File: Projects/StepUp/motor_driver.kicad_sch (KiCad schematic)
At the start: 39 parts, among them J5 TBLH10-350-04BK, Q1 BSS84, Q2 2N7002, U4 TMC2300-LA

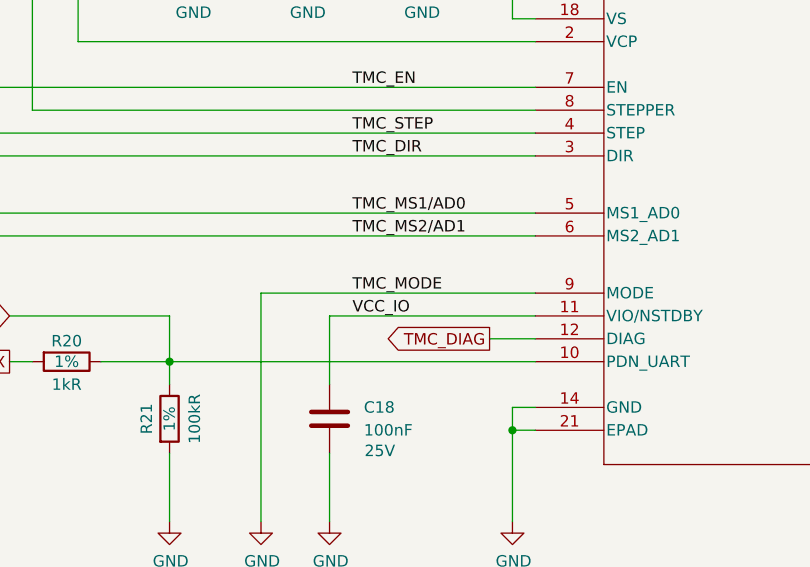
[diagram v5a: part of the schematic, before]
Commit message: chore(pins): MCU_BOOST_EN to MCU, fixed errors
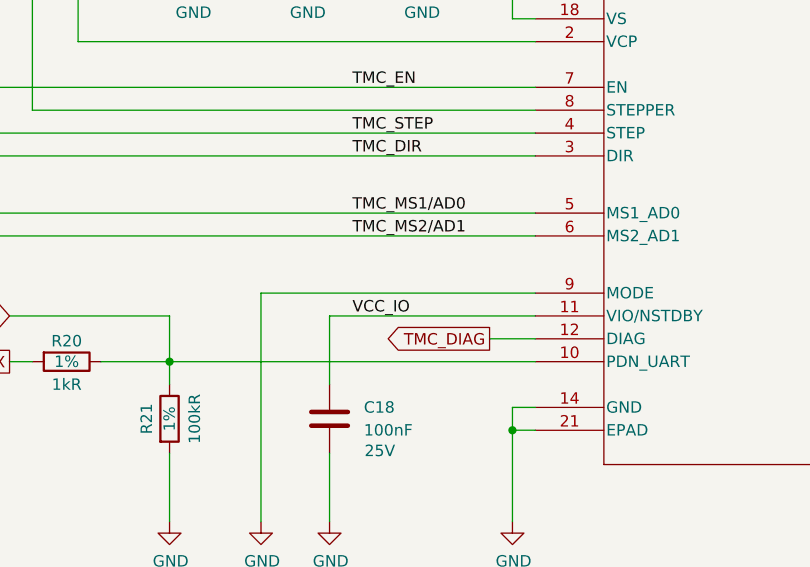
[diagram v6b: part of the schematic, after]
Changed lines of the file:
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@@
 		)
 	)
-	(label "TMC_MODE"
-		(at 124.46 177.8 0)
-		(fields_autoplaced yes)
-		(effects
-			(font
-				(size 1.27 1.27)
-			)
-			(justify left bottom)
-		)
-	)
 	(label "OB1_OUT"
 		(at 307.34 160.02 0)
@@
 			(font
 				(size 1.27 1.27)
+				(color 194 0 194 1)
 			)
 			(justify right)
@@
 			(font
 				(size 1.27 1.27)
+				(color 194 0 194 1)
 			)
 			(justify right)
@@
 			(font
 				(size 1.27 1.27)
+				(color 194 0 194 1)
 			)
 			(justify right)
@@
 			(font
 				(size 1.27 1.27)
+				(color 194 0 194 1)
 			)
 			(justify right)
@@
 			(font
 				(size 1.27 1.27)
+				(color 194 0 194 1)
 			)
 			(justify right)
@@
 			(font
 				(size 1.27 1.27)
+				(color 194 0 194 1)
 			)
 			(justify right)
@@
 			(font
 				(size 1.27 1.27)
+				(color 194 0 194 1)
 			)
 			(justify right)
@@
 			)
 		)
-		(property "Description" ""
+		(property "Description" "Power symbol creates a global label with name \"GND\" , ground"
 			(at 132.08 142.24 0)
 			(effects
@@
 			)
 		)
-		(property "Description" ""
+		(property "Description" "Power symbol creates a global label with name \"GND\" , ground"
 			(at 76.2 86.36 0)
 			(effects
@@
 			)
 		)
-		(property "Description" ""
+		(property "Description" "Power symbol creates a global label with name \"GND\" , ground"
 			(at 114.3 203.2 0)
 			(effects
@@
 			)
 		)
-		(property "Description" ""
+		(property "Description" "Power symbol creates a global label with name \"GND\" , ground"
 			(at 63.5 86.36 0)
 			(effects
@@
 			)
 		)
-		(property "Description" ""
+		(property "Description" "Power symbol creates a global label with name \"GND\" , ground"
 			(at 63.5 190.5 0)
 			(effects
@@
 			)
 		)
-		(property "Description" ""
+		(property "Description" "Power symbol creates a global label with name \"GND\" , ground"
 			(at 119.38 142.24 0)
 			(effects
@@
 			)
 		)
-		(property "Description" ""
+		(property "Description" "Power symbol creates a global label with name \"GND\" , ground"
 			(at 264.16 154.94 0)
 			(effects
@@
 			)
 		)
-		(property "Description" ""
+		(property "Description" "Power symbol creates a global label with name \"GND\" , ground"
 			(at 104.14 203.2 0)
 			(effects
@@
 			)
 		)
-		(property "Description" ""
+		(property "Description" "Power symbol creates a global label with name \"GND\" , ground"
 			(at 269.24 185.42 0)
 			(effects
@@
 			)
 		)
-		(property "Description" ""
+		(property "Description" "Power symbol creates a global label with name \"GND\" , ground"
 			(at 358.14 182.88 0)
 			(effects
@@
 			)
 		)
+		(property "Description" "MOSFET P-CH 50V 130MA SOT-23"
+			(at 35.56 40.64 0)
+			(effects
+				(font
+					(size 1.524 1.524)
+				)
+				(justify left)
+				(hide yes)
+			)
+		)
 		(pin "3"
 		)
@@
 			)
 		)
-		(property "Description" ""
+		(property "Description" "Power symbol creates a global label with name \"GND\" , ground"
 			(at 121.92 203.2 0)
 			(effects
@@
 			)
 		)
-		(property "Description" ""
+		(property "Description" "Power symbol creates a global label with name \"GND\" , ground"
 			(at 330.2 182.88 0)
 			(effects
@@
 			)
 		)
-		(property "Description" ""
+		(property "Description" "Power symbol creates a global label with name \"GND\" , ground"
 			(at 58.42 190.5 0)
 			(effects
@@
 			)
 		)
-		(property "Description" ""
+		(property "Description" "Power symbol creates a global label with name \"VBUS\""
 			(at 88.9 124.46 0)
 			(effects
@@
 			)
 		)
-		(property "Description" ""
+		(property "Description" "Power symbol creates a global label with name \"GND\" , ground"
 			(at 347.98 182.88 0)
 			(effects
@@
 			)
 		)
-		(property "Description" ""
+		(property "Description" "Power symbol creates a global label with name \"GND\" , ground"
 			(at 228.6 154.94 0)
 			(effects
@@
 			)
 		)
-		(property "Description" ""
+		(property "Description" "Power symbol creates a global label with name \"GND\" , ground"
 			(at 142.24 203.2 0)
 			(effects
@@
 			)
 		)
-		(property "Description" ""
+		(property "Description" "Power symbol creates a global label with name \"VBUS\""
 			(at 340.36 129.54 0)
 			(effects
@@
 			)
 		)
-		(property "Description" ""
+		(property "Description" "Power symbol creates a global label with name \"+3V3\""
 			(at 38.1 44.45 0)
 			(effects
@@
 			)
 		)
-		(property "Description" ""
+		(property "Description" "Power symbol creates a global label with name \"GND\" , ground"
 			(at 269.24 127 0)
 			(effects
@@
 			)
 		)
-		(property "Description" ""
+		(property "Description" "Power symbol creates a global label with name \"GND\" , ground"
 			(at 228.6 170.18 0)
 			(effects
@@
 			)
 		)
-		(property "Description" ""
+		(property "Description" "Power symbol creates a global label with name \"VBUS\""
 			(at 358.14 129.54 0)
 			(effects
@@
 			)
 		)
-		(property "Description" ""
+		(property "Description" "Power symbol creates a global label with name \"GND\" , ground"
 			(at 106.68 142.24 0)
 			(effects
@@
 			)
 		)
-		(property "Description" ""
+		(property "Description" "Power symbol creates a global label with name \"GND\" , ground"
 			(at 340.36 182.88 0)
 			(effects
@@
 			)
 		)
-		(property "Description" ""
+		(property "Description" "Power symbol creates a global label with name \"VBUS\""
 			(at 347.98 129.54 0)
 			(effects
@@
 			)
 		)
-		(property "Description" ""
+		(property "Description" "Power symbol creates a global label with name \"GND\" , ground"
 			(at 210.82 203.2 0)
 			(effects
@@
 			)
 		)
-		(property "Description" ""
+		(property "Description" "Power symbol creates a global label with name \"GND\" , ground"
 			(at 53.34 190.5 0)
 			(effects
@@
 			)
 		)
-		(property "Description" ""
+		(property "Description" "Power symbol creates a global label with name \"GND\" , ground"
 			(at 50.8 86.36 0)
 			(effects
@@
 			)
 		)
+		(property "Description" "MOSFET N-CH 60V 115MA SOT-23"
+			(at 68.58 40.64 0)
+			(effects
+				(font
+					(size 1.524 1.524)
+				)
+				(justify left)
+				(hide yes)
+			)
+		)
 		(pin "1"
 		)
@@
 			)
 		)
-		(property "Description" ""
+		(property "Description" "Power symbol creates a global label with name \"VBUS\""
 			(at 330.2 129.54 0)
 			(effects

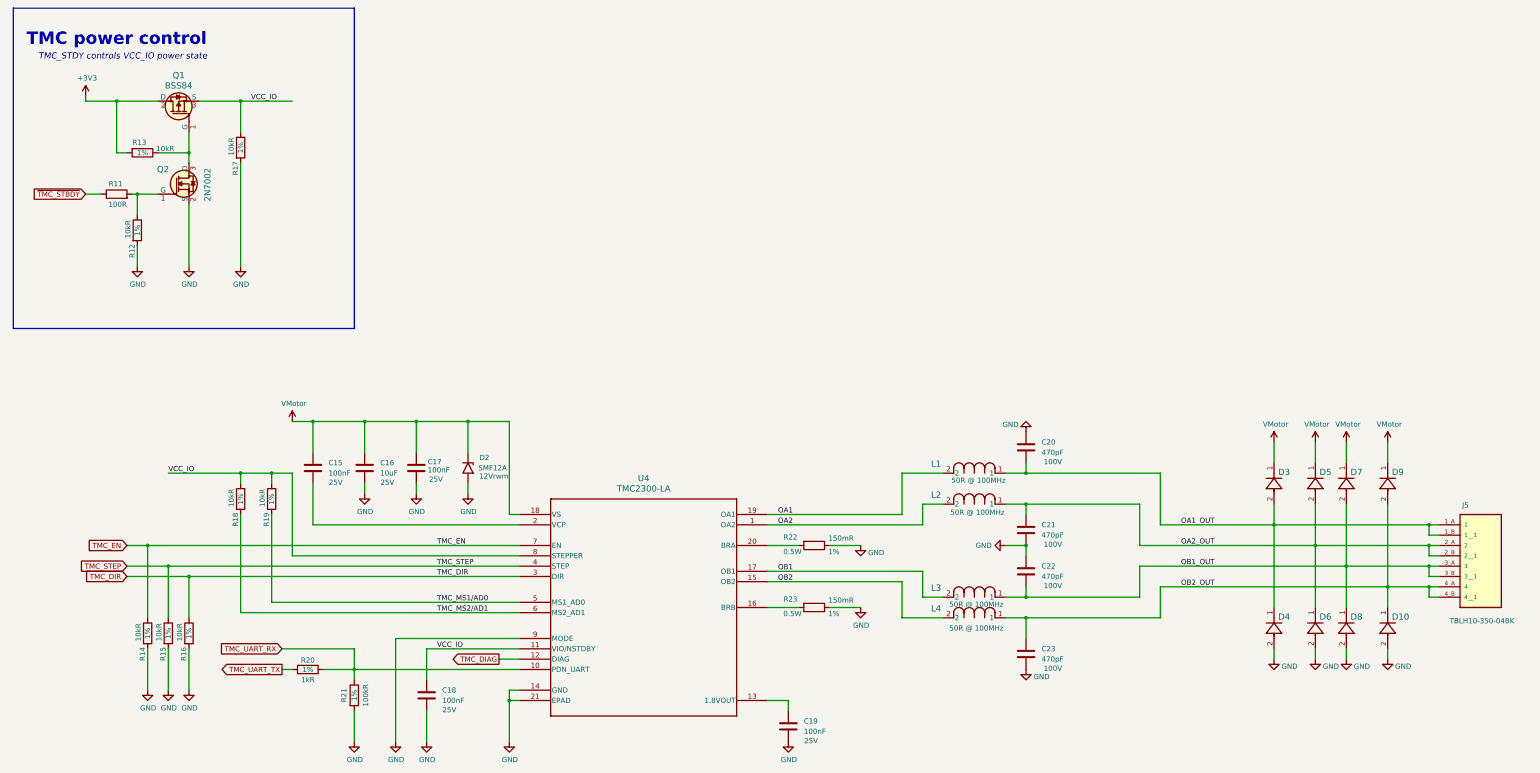
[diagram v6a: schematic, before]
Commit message: feat(layout): Blocks organised
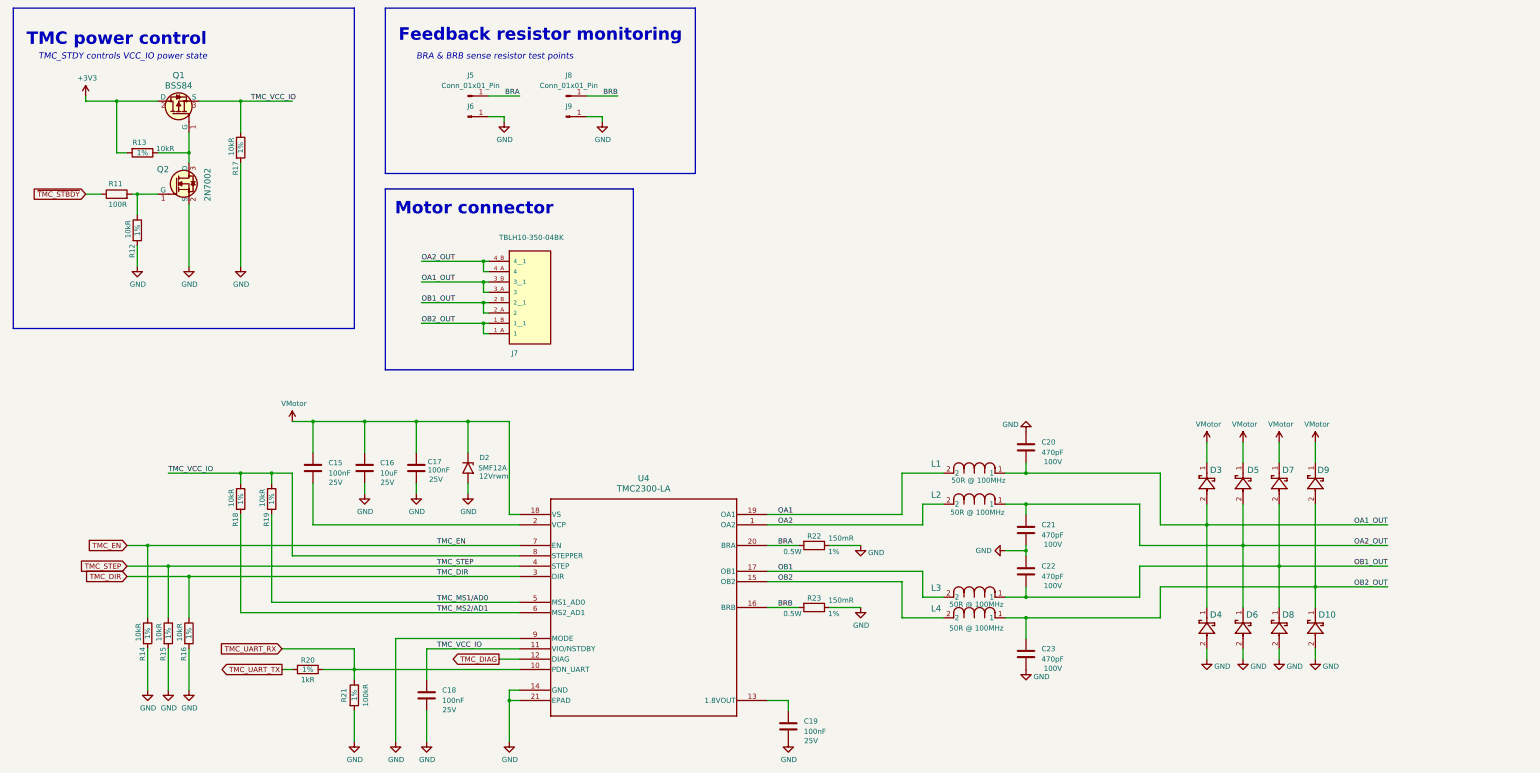
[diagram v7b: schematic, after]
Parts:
- removed D10, D3, D4, D5, D6, D7, D8, D9: SSA33L-E3/61T, Snapeda:DIODE_DO214AC, symbol Snapeda_kicad_2:SSA33L-E3_61T
- removed J5: TBLH10-350-04BK, Snapeda:CUI_TBLH10-350-04BK, symbol Snapeda:TBLH10-350-04BK
- added D10, D3, D4, D5, D6, D7, D8, D9: B5819W-TP, Snapeda:SDO_SOD-123_MCC, symbol Snapeda_kicad_2:B5819W-TP
- added J5, J6, J8, J9: Conn_01x01_Pin, Connector_PinHeader_2.54mm:PinHeader_1x01_P2.54mm_Vertical, symbol Connector:Conn_01x01_Pin
- added J7: TBLH10-350-04BK, Snapeda:CUI_TBLH10-350-04BK, symbol Snapeda:TBLH10-350-04BK
- C15, C17, C18, C19, C20, C21, C22, C23: footprint Capacitor_SMD:C_0603_1608Metric -> Capacitor_SMD:C_0402_1005Metric
- C16: footprint Capacitor_SMD:C_0805_2012Metric -> Capacitor_SMD:C_0603_1608Metric
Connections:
- net GND: now also D10.2, D4.2, D6.2, D8.2, J6.1 (Pin_1), J9.1 (Pin_1)
- net OA1_OUT: now also D3.2, D4.1, J7.3_A (3), J7.3_B (3__1)
- net OA2_OUT: now also D5.2, D6.1, J7.4_A (4), J7.4_B (4__1)
- net OB1_OUT: now also D7.2, D8.1, J7.2_A (2), J7.2_B (2__1)
- net OB2_OUT: now also D10.1, D9.2, J7.1_A (1), J7.1_B (1__1)
- net VMotor: now also D3.1, D5.1, D7.1, D9.1
- net BRB: now reaches R23.2, U4.16 (BRB)
- net BRB: now also J8.1 (Pin_1)
- net BRA: now reaches R22.2, U4.20 (BRA)
- net BRA: now also J5.1 (Pin_1)
- net VCC_IO renamed TMC_VCC_IO
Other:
- note added: "BRA & BRB sense resistor test points"
- note added: "Feedback resistor monitoring"
- note added: "Motor connector"

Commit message: feat(tidy): Bigger PMOS, added footprints
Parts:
- renumbered R13 to R10, R14 to R11, R15 to R12, R16 to R13, R17 to R14, R18 to R15, R19 to R16, R20 to R17, R21 to R18, R22 to R19, R23 to R20, R11 to R8, R12 to R9
